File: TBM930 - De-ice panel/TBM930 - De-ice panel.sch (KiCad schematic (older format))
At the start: 69 parts, among them J1 SW_AIRFRAME_DE_ICE, J10 AVR-ISP-6, J11 Screw_Terminal_01x02, J2 SW_ICE_LIGHT, J3 SW_PROP_DE_ICE, J4 SW_WIND_SHIELD, J5 SW_PITOT_L_HTR, J6 SW_PITOT_R_HTR, J7 SW_INERT_SEP, J8 Barrel_Jack, J9 USB_B_Micro, SW1 SW_Push, SW2 SW_Push, U1 TLC5917IN, U2 TLC5917IN, U3 ATmega32U4-MU, Y1 Crystal_GND24

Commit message: More footprint changes
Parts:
- C11: value 0.1uf -> 100nf; footprint Capacitor_SMD:C_0603_1608Metric -> Capacitor_SMD:C_0402_1005Metric; JLC 0603 -> 0402; LCSC C14663 -> C1525
- C12, C2, C3, C4, C5, C8, C9: value 0.1uF -> 100nf; footprint Capacitor_SMD:C_0603_1608Metric -> Capacitor_SMD:C_0402_1005Metric; JLC 0603 -> 0402; LCSC C14663 -> C1525
- C6, C7: footprint Capacitor_SMD:C_0603_1608Metric -> Capacitor_SMD:C_0402_1005Metric; JLC 0603 -> 0402; LCSC C15849 -> C52923
- R10, R11: footprint Resistor_SMD:R_0603_1608Metric -> Resistor_SMD:R_0402_1005Metric; JLC 0603 -> 0402; LCSC C25804 -> C25744
- R2, R5, R9: footprint Resistor_SMD:R_0603_1608Metric -> Resistor_SMD:R_0402_1005Metric; JLC 0603 -> 0402; LCSC C23138 -> C25104
- R3, R4: footprint Resistor_SMD:R_0603_1608Metric -> Resistor_THT:R_Axial_DIN0207_L6.3mm_D2.5mm_P7.62mm_Horizontal; JLC 0603 -> (none); LCSC C21190 -> (none)
- R6: footprint Resistor_SMD:R_0603_1608Metric -> Resistor_SMD:R_0402_1005Metric; JLC 0603 -> (none); LCSC C21190 -> C11702
- R7, R8: footprint Resistor_SMD:R_0603_1608Metric -> Resistor_SMD:R_0402_1005Metric; JLC 0603 -> 0402; LCSC C23345 -> C25092
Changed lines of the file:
@@
 P 8250 2100
 F 0 "C9" H 8500 2050 50  0000 R CNN
-F 1 "0.1uF" H 8600 2150 50  0000 R CNN
-F 2 "Capacitor_SMD:C_0603_1608Metric" H 8288 1950 50  0001 C CNN
+F 1 "100nf" H 8600 2150 50  0000 R CNN
+F 2 "Capacitor_SMD:C_0402_1005Metric" H 8288 1950 50  0001 C CNN
 F 3 "~" H 8250 2100 50  0001 C CNN
-F 4 "0603" H 8250 2100 50  0001 C CNN "JLC"
-F 5 "C14663" H 8250 2100 50  0001 C CNN "LCSC"
+F 4 "0402" H 8250 2100 50  0001 C CNN "JLC"
+F 5 "C1525" H 8250 2100 50  0001 C CNN "LCSC"
 	1    8250 2100
 	-1   0    0    1
@@
 F 0 "R4" V 6193 1700 50  0000 C CNN
 F 1 "1k" V 6284 1700 50  0000 C CNN
-F 2 "Resistor_SMD:R_0603_1608Metric" V 6330 1700 50  0001 C CNN
+F 2 "Resistor_THT:R_Axial_DIN0207_L6.3mm_D2.5mm_P7.62mm_Horizontal" V 6330 1700 50  0001 C CNN
 F 3 "~" H 6400 1700 50  0001 C CNN
-F 4 "0603" H 6400 1700 50  0001 C CNN "JLC"
-F 5 "C21190" H 6400 1700 50  0001 C CNN "LCSC"
+F 4 "" H 6400 1700 50  0001 C CNN "JLC"
+F 5 "" H 6400 1700 50  0001 C CNN "LCSC"
 	1    6400 1700
 	-1   0    0    1
@@
 F 0 "R6" H 2620 5746 50  0000 L CNN
 F 1 "1K" H 2620 5655 50  0000 L CNN
-F 2 "Resistor_SMD:R_0603_1608Metric" V 2480 5700 50  0001 C CNN
+F 2 "Resistor_SMD:R_0402_1005Metric" V 2480 5700 50  0001 C CNN
 F 3 "~" H 2550 5700 50  0001 C CNN
-F 4 "0603" H 2550 5700 50  0001 C CNN "JLC"
-F 5 "C21190" H 2550 5700 50  0001 C CNN "LCSC"
+F 4 "" H 2550 5700 50  0001 C CNN "JLC"
+F 5 "C11702" H 2550 5700 50  0001 C CNN "LCSC"
 	1    2550 5700
 	1    0    0    -1
@@
 F 0 "C6" H 765 2246 50  0000 L CNN
 F 1 "1uF" H 765 2155 50  0000 L CNN
-F 2 "Capacitor_SMD:C_0603_1608Metric" H 688 2050 50  0001 C CNN
+F 2 "Capacitor_SMD:C_0402_1005Metric" H 688 2050 50  0001 C CNN
 F 3 "~" H 650 2200 50  0001 C CNN
-F 4 "0603" H 650 2200 50  0001 C CNN "JLC"
-F 5 "C15849" H 650 2200 50  0001 C CNN "LCSC"
+F 4 "0402" H 650 2200 50  0001 C CNN "JLC"
+F 5 "C52923" H 650 2200 50  0001 C CNN "LCSC"
 	1    650  2200
 	1    0    0    -1
@@
 F 0 "R5" H 3530 3254 50  0000 R CNN
 F 1 "330" H 3530 3345 50  0000 R CNN
-F 2 "Resistor_SMD:R_0603_1608Metric" V 3530 3300 50  0001 C CNN
+F 2 "Resistor_SMD:R_0402_1005Metric" V 3530 3300 50  0001 C CNN
 F 3 "~" H 3600 3300 50  0001 C CNN
-F 4 "0603" H 3600 3300 50  0001 C CNN "JLC"
-F 5 "C23138" H 3600 3300 50  0001 C CNN "LCSC"
+F 4 "0402" H 3600 3300 50  0001 C CNN "JLC"
+F 5 "C25104" H 3600 3300 50  0001 C CNN "LCSC"
 	1    3600 3300
 	-1   0    0    1
@@
 F 0 "R2" H 3670 1646 50  0000 L CNN
 F 1 "330" H 3670 1555 50  0000 L CNN
-F 2 "Resistor_SMD:R_0603_1608Metric" V 3530 1600 50  0001 C CNN
+F 2 "Resistor_SMD:R_0402_1005Metric" V 3530 1600 50  0001 C CNN
 F 3 "~" H 3600 1600 50  0001 C CNN
-F 4 "0603" H 3600 1600 50  0001 C CNN "JLC"
-F 5 "C23138" H 3600 1600 50  0001 C CNN "LCSC"
+F 4 "0402" H 3600 1600 50  0001 C CNN "JLC"
+F 5 "C25104" H 3600 1600 50  0001 C CNN "LCSC"
 	1    3600 1600
 	1    0    0    -1
@@
 P 2600 1000
 F 0 "C2" H 2715 1046 50  0000 L CNN
-F 1 "0.1uF" H 2715 955 50  0000 L CNN
-F 2 "Capacitor_SMD:C_0603_1608Metric" H 2638 850 50  0001 C CNN
+F 1 "100nf" H 2715 955 50  0000 L CNN
+F 2 "Capacitor_SMD:C_0402_1005Metric" H 2638 850 50  0001 C CNN
 F 3 "~" H 2600 1000 50  0001 C CNN
-F 4 "0603" H 2600 1000 50  0001 C CNN "JLC"
-F 5 "C14663" H 2600 1000 50  0001 C CNN "LCSC"
+F 4 "0402" H 2600 1000 50  0001 C CNN "JLC"
+F 5 "C1525" H 2600 1000 50  0001 C CNN "LCSC"
 	1    2600 1000
 	1    0    0    -1
@@
 P 3050 1000
 F 0 "C3" H 3165 1046 50  0000 L CNN
-F 1 "0.1uF" H 3165 955 50  0000 L CNN
-F 2 "Capacitor_SMD:C_0603_1608Metric" H 3088 850 50  0001 C CNN
+F 1 "100nf" H 3165 955 50  0000 L CNN
+F 2 "Capacitor_SMD:C_0402_1005Metric" H 3088 850 50  0001 C CNN
 F 3 "~" H 3050 1000 50  0001 C CNN
-F 4 "0603" H 3050 1000 50  0001 C CNN "JLC"
-F 5 "C14663" H 3050 1000 50  0001 C CNN "LCSC"
+F 4 "0402" H 3050 1000 50  0001 C CNN "JLC"
+F 5 "C1525" H 3050 1000 50  0001 C CNN "LCSC"
 	1    3050 1000
 	1    0    0    -1
@@
 P 3500 1000
 F 0 "C4" H 3615 1046 50  0000 L CNN
-F 1 "0.1uF" H 3615 955 50  0000 L CNN
-F 2 "Capacitor_SMD:C_0603_1608Metric" H 3538 850 50  0001 C CNN
+F 1 "100nf" H 3615 955 50  0000 L CNN
+F 2 "Capacitor_SMD:C_0402_1005Metric" H 3538 850 50  0001 C CNN
 F 3 "~" H 3500 1000 50  0001 C CNN
-F 4 "0603" H 3500 1000 50  0001 C CNN "JLC"
-F 5 "C14663" H 3500 1000 50  0001 C CNN "LCSC"
+F 4 "0402" H 3500 1000 50  0001 C CNN "JLC"
+F 5 "C1525" H 3500 1000 50  0001 C CNN "LCSC"
 	1    3500 1000
 	1    0    0    -1
@@
 P 3950 1000
 F 0 "C5" H 4065 1046 50  0000 L CNN
-F 1 "0.1uF" H 4065 955 50  0000 L CNN
-F 2 "Capacitor_SMD:C_0603_1608Metric" H 3988 850 50  0001 C CNN
+F 1 "100nf" H 4065 955 50  0000 L CNN
+F 2 "Capacitor_SMD:C_0402_1005Metric" H 3988 850 50  0001 C CNN
 F 3 "~" H 3950 1000 50  0001 C CNN
-F 4 "0603" H 3950 1000 50  0001 C CNN "JLC"
-F 5 "C14663" H 3950 1000 50  0001 C CNN "LCSC"
+F 4 "0402" H 3950 1000 50  0001 C CNN "JLC"
+F 5 "C1525" H 3950 1000 50  0001 C CNN "LCSC"
 	1    3950 1000
 	1    0    0    -1
@@
 F 0 "R8" V 1707 6250 50  0000 C CNN
 F 1 "22" V 1616 6250 50  0000 C CNN
-F 2 "Resistor_SMD:R_0603_1608Metric" V 1430 6250 50  0001 C CNN
+F 2 "Resistor_SMD:R_0402_1005Metric" V 1430 6250 50  0001 C CNN
 F 3 "~" H 1500 6250 50  0001 C CNN
-F 4 "0603" H 1500 6250 50  0001 C CNN "JLC"
-F 5 "C23345" H 1500 6250 50  0001 C CNN "LCSC"
+F 4 "0402" H 1500 6250 50  0001 C CNN "JLC"
+F 5 "C25092" H 1500 6250 50  0001 C CNN "LCSC"
 	1    1500 6250
 	0    -1   -1   0
@@
 F 0 "C7" H 1065 2946 50  0000 L CNN
 F 1 "1uF" H 1065 2855 50  0000 L CNN
-F 2 "Capacitor_SMD:C_0603_1608Metric" H 988 2750 50  0001 C CNN
+F 2 "Capacitor_SMD:C_0402_1005Metric" H 988 2750 50  0001 C CNN
 F 3 "~" H 950 2900 50  0001 C CNN
-F 4 "0603" H 950 2900 50  0001 C CNN "JLC"
-F 5 "C15849" H 950 2900 50  0001 C CNN "LCSC"
+F 4 "0402" H 950 2900 50  0001 C CNN "JLC"
+F 5 "C52923" H 950 2900 50  0001 C CNN "LCSC"
 	1    950  2900
 	1    0    0    -1
@@
 F 0 "R7" V 1707 5900 50  0000 C CNN
 F 1 "22" V 1616 5900 50  0000 C CNN
-F 2 "Resistor_SMD:R_0603_1608Metric" V 1430 5900 50  0001 C CNN
+F 2 "Resistor_SMD:R_0402_1005Metric" V 1430 5900 50  0001 C CNN
 F 3 "~" H 1500 5900 50  0001 C CNN
-F 4 "0603" H 1500 5900 50  0001 C CNN "JLC"
-F 5 "C23345" H 1500 5900 50  0001 C CNN "LCSC"
+F 4 "0402" H 1500 5900 50  0001 C CNN "JLC"
+F 5 "C25092" H 1500 5900 50  0001 C CNN "LCSC"
 	1    1500 5900
 	0    -1   -1   0
@@
 F 0 "R9" V 4843 7300 50  0000 C CNN
 F 1 "330" V 4934 7300 50  0000 C CNN
-F 2 "Resistor_SMD:R_0603_1608Metric" V 4980 7300 50  0001 C CNN
+F 2 "Resistor_SMD:R_0402_1005Metric" V 4980 7300 50  0001 C CNN
 F 3 "~" H 5050 7300 50  0001 C CNN
-F 4 "0603" H 5050 7300 50  0001 C CNN "JLC"
-F 5 "C23138" H 5050 7300 50  0001 C CNN "LCSC"
+F 4 "0402" H 5050 7300 50  0001 C CNN "JLC"
+F 5 "C25104" H 5050 7300 50  0001 C CNN "LCSC"
 	1    5050 7300
 	0    1    1    0
@@
 F 0 "R10" H 5270 6546 50  0000 L CNN
 F 1 "10K" H 5270 6455 50  0000 L CNN
-F 2 "Resistor_SMD:R_0603_1608Metric" V 5130 6500 50  0001 C CNN
+F 2 "Resistor_SMD:R_0402_1005Metric" V 5130 6500 50  0001 C CNN
 F 3 "~" H 5200 6500 50  0001 C CNN
-F 4 "0603" H 5200 6500 50  0001 C CNN "JLC"
-F 5 "C25804" H 5200 6500 50  0001 C CNN "LCSC"
+F 4 "0402" H 5200 6500 50  0001 C CNN "JLC"
+F 5 "C25744" H 5200 6500 50  0001 C CNN "LCSC"
 	1    5200 6500
 	1    0    0    -1
@@
 P 5700 6500
 F 0 "C11" H 5815 6546 50  0000 L CNN
-F 1 "0.1uf" H 5815 6455 50  0000 L CNN
-F 2 "Capacitor_SMD:C_0603_1608Metric" H 5738 6350 50  0001 C CNN
+F 1 "100nf" H 5815 6455 50  0000 L CNN
+F 2 "Capacitor_SMD:C_0402_1005Metric" H 5738 6350 50  0001 C CNN
 F 3 "~" H 5700 6500 50  0001 C CNN
-F 4 "0603" H 5700 6500 50  0001 C CNN "JLC"
-F 5 "C14663" H 5700 6500 50  0001 C CNN "LCSC"
+F 4 "0402" H 5700 6500 50  0001 C CNN "JLC"
+F 5 "C1525" H 5700 6500 50  0001 C CNN "LCSC"
 	1    5700 6500
 	1    0    0    -1
@@
 P 6150 6500
 F 0 "C12" H 6265 6546 50  0000 L CNN
-F 1 "0.1uF" H 6265 6455 50  0000 L CNN
-F 2 "Capacitor_SMD:C_0603_1608Metric" H 6188 6350 50  0001 C CNN
+F 1 "100nf" H 6265 6455 50  0000 L CNN
+F 2 "Capacitor_SMD:C_0402_1005Metric" H 6188 6350 50  0001 C CNN
 F 3 "~" H 6150 6500 50  0001 C CNN
-F 4 "0603" H 6150 6500 50  0001 C CNN "JLC"
-F 5 "C14663" H 6150 6500 50  0001 C CNN "LCSC"
+F 4 "0402" H 6150 6500 50  0001 C CNN "JLC"
+F 5 "C1525" H 6150 6500 50  0001 C CNN "LCSC"
 	1    6150 6500
 	1    0    0    -1
@@
 F 0 "R11" V 2950 3550 50  0000 C CNN
 F 1 "10K" V 2850 3550 50  0000 C CNN
-F 2 "Resistor_SMD:R_0603_1608Metric" V 2980 3550 50  0001 C CNN
+F 2 "Resistor_SMD:R_0402_1005Metric" V 2980 3550 50  0001 C CNN
 F 3 "~" H 3050 3550 50  0001 C CNN
-F 4 "0603" H 3050 3550 50  0001 C CNN "JLC"
-F 5 "C25804" H 3050 3550 50  0001 C CNN "LCSC"
+F 4 "0402" H 3050 3550 50  0001 C CNN "JLC"
+F 5 "C25744" H 3050 3550 50  0001 C CNN "LCSC"
 	1    3050 3550
 	0    -1   -1   0
@@
 F 0 "R3" V 9143 1700 50  0000 C CNN
 F 1 "1k" V 9234 1700 50  0000 C CNN
-F 2 "Resistor_SMD:R_0603_1608Metric" V 9280 1700 50  0001 C CNN
+F 2 "Resistor_THT:R_Axial_DIN0207_L6.3mm_D2.5mm_P7.62mm_Horizontal" V 9280 1700 50  0001 C CNN
 F 3 "~" H 9350 1700 50  0001 C CNN
-F 4 "0603" H 9350 1700 50  0001 C CNN "JLC"
-F 5 "C21190" H 9350 1700 50  0001 C CNN "LCSC"
+F 4 "" H 9350 1700 50  0001 C CNN "JLC"
+F 5 "" H 9350 1700 50  0001 C CNN "LCSC"
 	1    9350 1700
 	-1   0    0    1
@@
 P 8600 1750
 F 0 "C8" H 8485 1704 50  0000 R CNN
-F 1 "0.1uF" H 8485 1795 50  0000 R CNN
-F 2 "Capacitor_SMD:C_0603_1608Metric" H 8638 1600 50  0001 C CNN
+F 1 "100nf" H 8485 1795 50  0000 R CNN
+F 2 "Capacitor_SMD:C_0402_1005Metric" H 8638 1600 50  0001 C CNN
 F 3 "~" H 8600 1750 50  0001 C CNN
-F 4 "0603" H 8600 1750 50  0001 C CNN "JLC"
-F 5 "C14663" H 8600 1750 50  0001 C CNN "LCSC"
+F 4 "0402" H 8600 1750 50  0001 C CNN "JLC"
+F 5 "C1525" H 8600 1750 50  0001 C CNN "LCSC"
 	1    8600 1750
 	-1   0    0    1

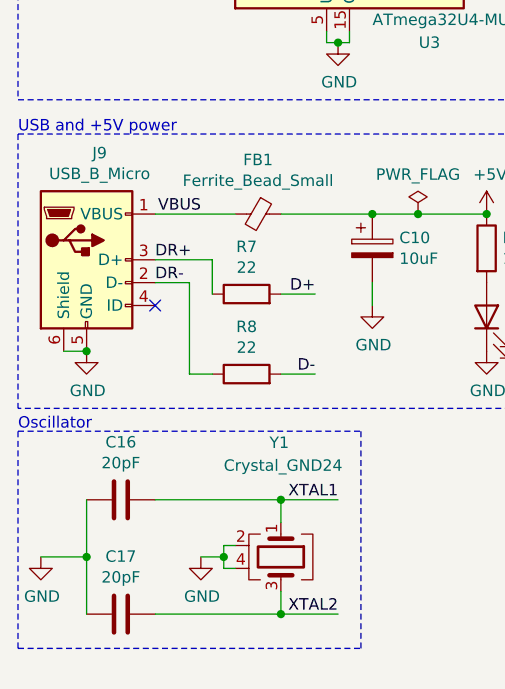
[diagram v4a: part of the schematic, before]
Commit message: Change connector, fix BOM
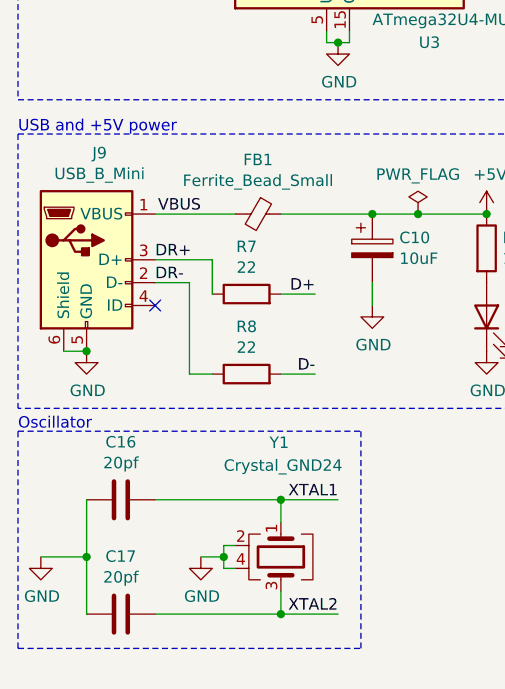
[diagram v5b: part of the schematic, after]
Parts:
- removed J9: USB_B_Micro, Global MobiFlight panel parts:USB_A_Molex_105057_Vertical, symbol Connector:USB_B_Micro
- added J9: USB_B_Mini, Global MobiFlight panel parts:USB_B_Mini_Amphenol_UE25BE5510H, symbol Connector:USB_B_Mini
- C1, C10: LCSC C15850 -> C19702
- C16, C17: value 20pF -> 20pf; LCSC C1555 -> C1554
- R6: JLC (none) -> 0402
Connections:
- net DR+: now also J9.3 (D+)
- net DR-: now also J9.2 (D-)
- net GND: now also J9.5 (GND), J9.6 (Shield)
- net VBUS: now also J9.1 (VBUS)
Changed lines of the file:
@@
 	8400 600  8400 5800
-$Comp
-L Connector:USB_B_Micro J9
-U 1 1 611C7326
-P 800 5750
-F 0 "J9" H 857 6217 50  0000 C CNN
-F 1 "USB_B_Micro" H 857 6126 50  0000 C CNN
-F 2 "Global MobiFlight panel parts:USB_A_Molex_105057_Vertical" H 950 5700 50  0001 C CNN
-F 3 "~" H 950 5700 50  0001 C CNN
-	1    800  5750
-	1    0    0    -1
-$EndComp
 $Comp
 L Device:CP C10
@@
 F 3 "~" H 2050 5700 50  0001 C CNN
 F 4 "0603" H 2050 5700 50  0001 C CNN "JLC"
-F 5 "C15850" H 2050 5700 50  0001 C CNN "LCSC"
+F 5 "C19702" H 2050 5700 50  0001 C CNN "LCSC"
 	1    2050 5700
 	1    0    0    -1
@@
 F 2 "Resistor_SMD:R_0402_1005Metric" V 2480 5700 50  0001 C CNN
 F 3 "~" H 2550 5700 50  0001 C CNN
-F 4 "" H 2550 5700 50  0001 C CNN "JLC"
+F 4 "0402" H 2550 5700 50  0001 C CNN "JLC"
 F 5 "C11702" H 2550 5700 50  0001 C CNN "LCSC"
 	1    2550 5700
@@
 P 950 6800
 F 0 "C16" V 698 6800 50  0000 C CNN
-F 1 "20pF" V 789 6800 50  0000 C CNN
+F 1 "20pf" V 789 6800 50  0000 C CNN
 F 2 "Capacitor_SMD:C_0402_1005Metric" H 988 6650 50  0001 C CNN
 F 3 "~" H 950 6800 50  0001 C CNN
 F 4 "0402" H 950 6800 50  0001 C CNN "JLC"
-F 5 "C1555" H 950 6800 50  0001 C CNN "LCSC"
+F 5 "C1554" H 950 6800 50  0001 C CNN "LCSC"
 	1    950  6800
 	0    1    1    0
@@
 P 950 7300
 F 0 "C17" V 698 7300 50  0000 C CNN
-F 1 "20pF" V 789 7300 50  0000 C CNN
+F 1 "20pf" V 789 7300 50  0000 C CNN
 F 2 "Capacitor_SMD:C_0402_1005Metric" H 988 7150 50  0001 C CNN
 F 3 "~" H 950 7300 50  0001 C CNN
 F 4 "0402" H 950 7300 50  0001 C CNN "JLC"
-F 5 "C1555" H 950 7300 50  0001 C CNN "LCSC"
+F 5 "C1554" H 950 7300 50  0001 C CNN "LCSC"
 	1    950  7300
 	0    1    1    0
@@
 	1    0    0    -1
 $EndComp
-Connection ~ 800  6150
 $Comp
 L power:GND #PWR029
@@
 F 3 "~" H 1100 1000 50  0001 C CNN
 F 4 "0603" H 1100 1000 50  0001 C CNN "JLC"
-F 5 "C15850" H 1100 1000 50  0001 C CNN "LCSC"
+F 5 "C19702" H 1100 1000 50  0001 C CNN "LCSC"
 	1    1100 1000
 	1    0    0    -1
@@
 NoConn ~ 2750 4350
 NoConn ~ 7500 1550
+$Comp
+L Connector:USB_B_Mini J9
+U 1 1 61278480
+P 800 5750
+F 0 "J9" H 857 6217 50  0000 C CNN
+F 1 "USB_B_Mini" H 857 6126 50  0000 C CNN
+F 2 "Global MobiFlight panel parts:USB_B_Mini_Amphenol_UE25BE5510H" H 950 5700 50  0001 C CNN
+F 3 "~" H 950 5700 50  0001 C CNN
+	1    800  5750
+	1    0    0    -1
+$EndComp
+Connection ~ 800  6150
 $EndSCHEMATC
